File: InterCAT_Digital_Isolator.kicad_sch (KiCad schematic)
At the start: 21 parts

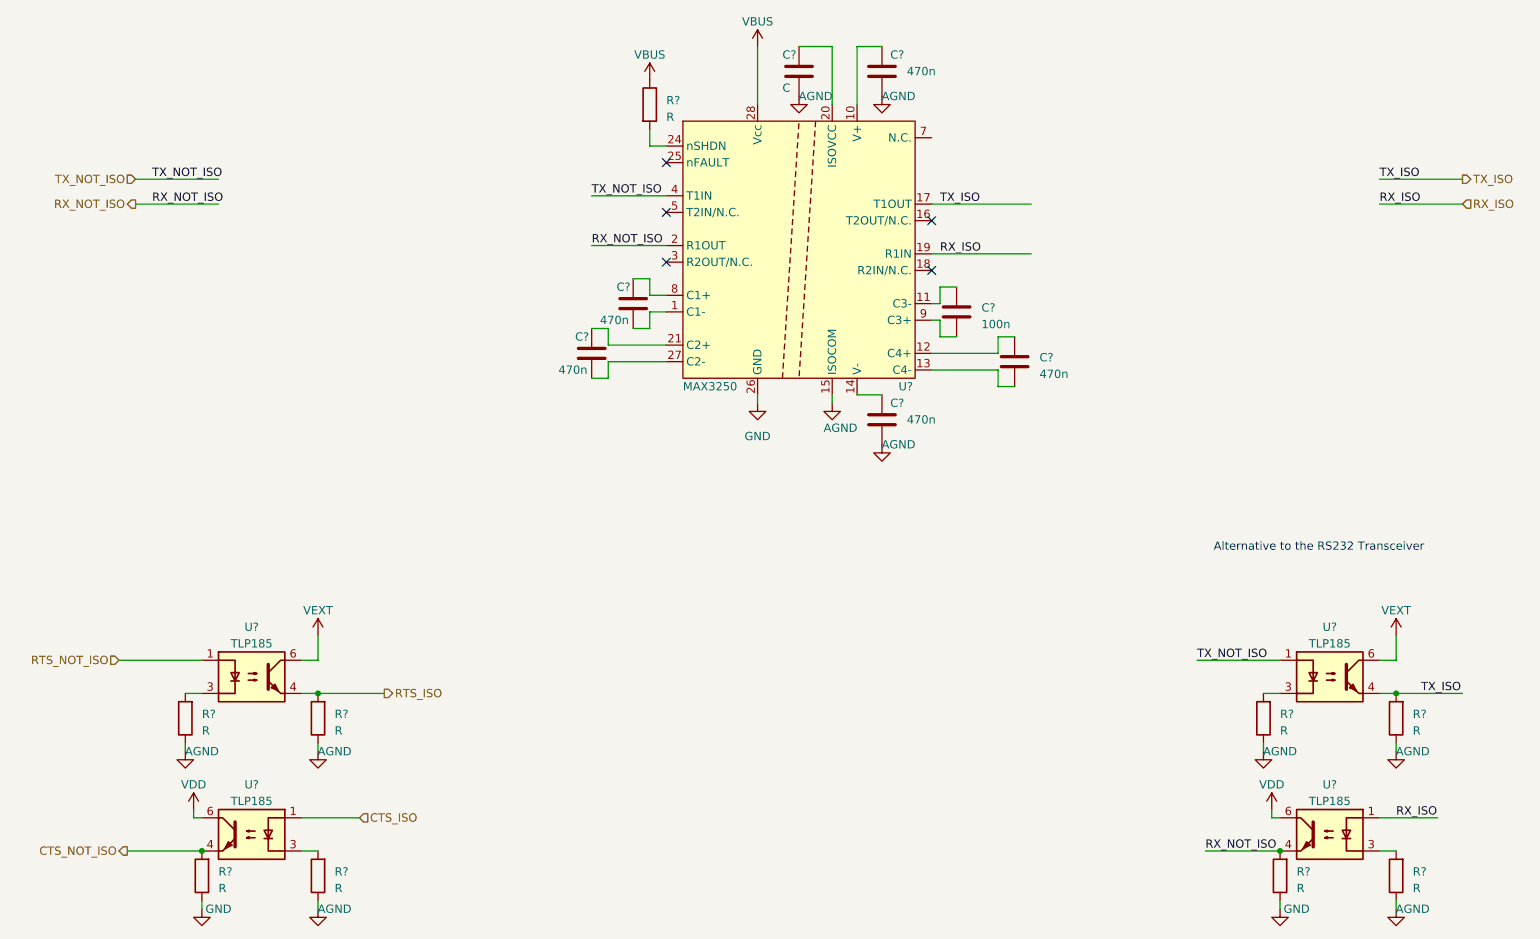
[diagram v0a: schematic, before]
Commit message: Started working on the PCB. alignement in analog channels. changed opamps ot Microchip RRIO basic on LCSC updated footprint on maxim Added LCSC parameter corrected some errors in GND/AGND corrected some errors in VCCA/VCC
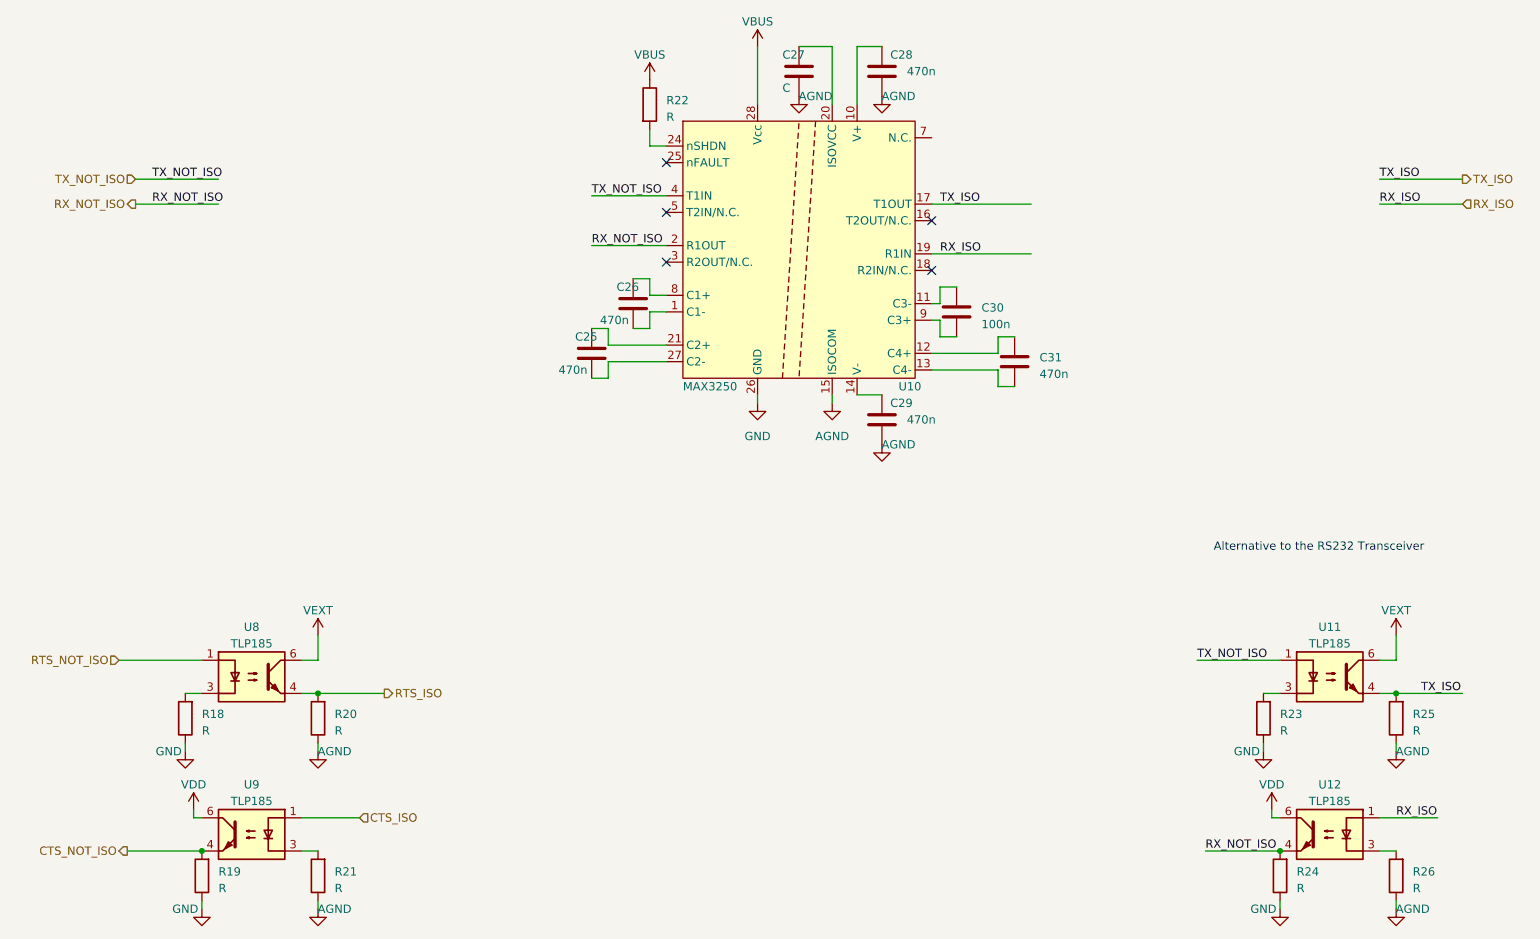
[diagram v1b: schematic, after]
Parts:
- C25, C26, C27, C28, C29, C30, C31: renamed from C?; footprint (none) -> Capacitor_SMD:C_0603_1608Metric
- R18, R19, R20, R21, R22, R23, R24, R25, R26: renamed from R?; footprint (none) -> Resistor_SMD:R_0603_1608Metric
- U10: renamed from U?; footprint Package_SO:SSOP-24_5.3x8.2mm_P0.65mm -> Package_SO:SSOP-28_5.3x10.2mm_P0.65mm
- gave numbers to parts that had none: 4
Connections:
- net GND: now also R18.1, R19.1, R23.1, R24.1; no longer U10.15 (ISOCOM)
- net GNDA: now also U10.15 (ISOCOM); no longer R18.1, R19.1, R23.1, R24.1

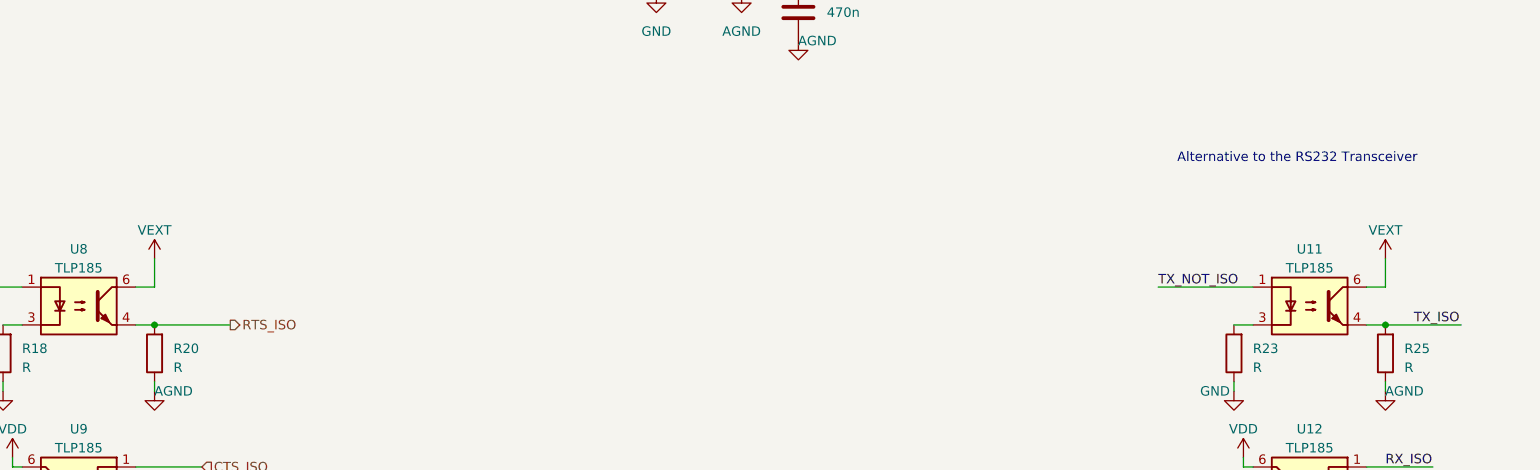
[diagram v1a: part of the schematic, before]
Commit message: Corrected hidden errors in power nets naming
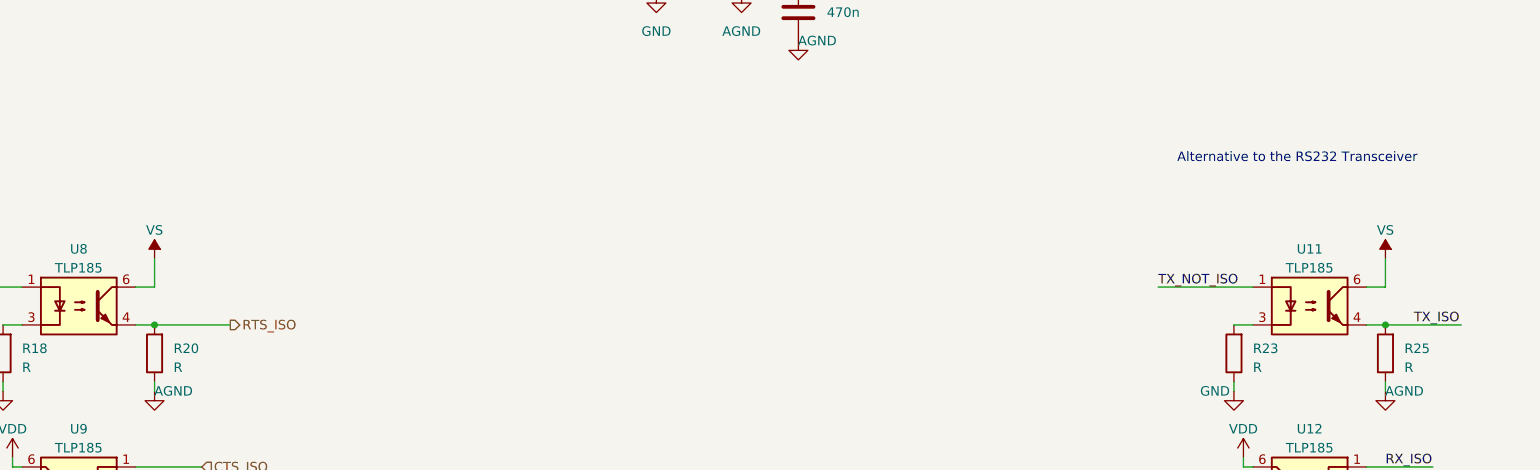
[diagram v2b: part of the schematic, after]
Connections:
- net VBUS: no longer U11.6, U8.6
- new net VS: U11.6, U8.6
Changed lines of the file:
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@@
+    )
+  )
+  (symbol (lib_id "power:VS") (at 243.84 116.84 0) (unit 1)
+    (in_bom yes) (on_board yes) (dnp no) (fields_autoplaced)
+    (property "Reference" "#PWR025" (at 238.76 120.65 0)
+      (effects (font (size 1.27 1.27)) hide)
+    )
+    (property "Value" "VS" (at 243.84 113.03 0)
+      (effects (font (size 1.27 1.27)))
+    )
+    (property "Footprint" "" (at 243.84 116.84 0)
+      (effects (font (size 1.27 1.27)) hide)
+    )
+    (property "Datasheet" "" (at 243.84 116.84 0)
+      (effects (font (size 1.27 1.27)) hide)
+    )
+    (pin "1")
+    (instances
+      (project "Intercat"
+        (path "/03d88a85-11fd-47aa-954c-c318bb15294a"
+          (reference "#PWR025") (unit 1)
+        )
+        (path "/03d88a85-11fd-47aa-954c-c318bb15294a/fcde6974-78be-43f2-8f1f-c3bd2febfa67"
+          (reference "#PWR028") (unit 1)
+        )
+      )
     )
   )
@@
   (symbol (lib_id "power:GND") (at 58.42 134.62 0) (unit 1)
     (in_bom yes) (on_board yes) (dnp no)
-    (property "Reference" "#PWR051" (at 58.42 140.97 0)
+    (property "Reference" "#PWR0133" (at 58.42 140.97 0)
       (effects (font (size 1.27 1.27)) hide)
     )
@@
       (project "Intercat"
         (path "/03d88a85-11fd-47aa-954c-c318bb15294a/fcde6974-78be-43f2-8f1f-c3bd2febfa67"
-          (reference "#PWR051") (unit 1)
+          (reference "#PWR0133") (unit 1)
         )
       )
@@
   (symbol (lib_id "power:GND") (at 226.06 158.75 0) (unit 1)
     (in_bom yes) (on_board yes) (dnp no)
-    (property "Reference" "#PWR066" (at 226.06 165.1 0)
+    (property "Reference" "#PWR0130" (at 226.06 165.1 0)
       (effects (font (size 1.27 1.27)) hide)
     )
@@
       (project "Intercat"
         (path "/03d88a85-11fd-47aa-954c-c318bb15294a/fcde6974-78be-43f2-8f1f-c3bd2febfa67"
-          (reference "#PWR066") (unit 1)
+          (reference "#PWR0130") (unit 1)
         )
       )
@@
   (symbol (lib_id "power:GND") (at 223.52 134.62 0) (unit 1)
     (in_bom yes) (on_board yes) (dnp no)
-    (property "Reference" "#PWR064" (at 223.52 140.97 0)
+    (property "Reference" "#PWR0131" (at 223.52 140.97 0)
       (effects (font (size 1.27 1.27)) hide)
     )
@@
       (project "Intercat"
         (path "/03d88a85-11fd-47aa-954c-c318bb15294a/fcde6974-78be-43f2-8f1f-c3bd2febfa67"
-          (reference "#PWR064") (unit 1)
+          (reference "#PWR0131") (unit 1)
         )
       )
@@
   (symbol (lib_id "power:GND") (at 146.05 81.28 0) (unit 1)
     (in_bom yes) (on_board yes) (dnp no) (fields_autoplaced)
-    (property "Reference" "#PWR059" (at 146.05 87.63 0)
+    (property "Reference" "#PWR0129" (at 146.05 87.63 0)
       (effects (font (size 1.27 1.27)) hide)
     )
@@
       (project "Intercat"
         (path "/03d88a85-11fd-47aa-954c-c318bb15294a/fcde6974-78be-43f2-8f1f-c3bd2febfa67"
-          (reference "#PWR059") (unit 1)
+          (reference "#PWR0129") (unit 1)
         )
       )
@@
     )
   )
-  (symbol (lib_id "power:VBUS") (at 243.84 116.84 0) (unit 1)
-    (in_bom yes) (on_board yes) (dnp no) (fields_autoplaced)
-    (property "Reference" "#PWR067" (at 243.84 120.65 0)
-      (effects (font (size 1.27 1.27)) hide)
-    )
-    (property "Value" "VEXT" (at 243.84 113.03 0)
-      (effects (font (size 1.27 1.27)))
-    )
-    (property "Footprint" "" (at 243.84 116.84 0)
-      (effects (font (size 1.27 1.27)) hide)
-    )
-    (property "Datasheet" "" (at 243.84 116.84 0)
-      (effects (font (size 1.27 1.27)) hide)
-    )
-    (pin "1")
-    (instances
-      (project "Intercat"
-        (path "/03d88a85-11fd-47aa-954c-c318bb15294a/fcde6974-78be-43f2-8f1f-c3bd2febfa67"
-          (reference "#PWR067") (unit 1)
-        )
-      )
-    )
-  )
   (symbol (lib_id "Device:R") (at 243.84 153.67 180) (unit 1)
     (in_bom yes) (on_board yes) (dnp no) (fields_autoplaced)
@@
         (path "/03d88a85-11fd-47aa-954c-c318bb15294a/fcde6974-78be-43f2-8f1f-c3bd2febfa67"
           (reference "C25") (unit 1)
-        )
-      )
-    )
-  )
-  (symbol (lib_id "power:VBUS") (at 78.74 116.84 0) (unit 1)
-    (in_bom yes) (on_board yes) (dnp no) (fields_autoplaced)
-    (property "Reference" "#PWR054" (at 78.74 120.65 0)
-      (effects (font (size 1.27 1.27)) hide)
-    )
-    (property "Value" "VEXT" (at 78.74 113.03 0)
-      (effects (font (size 1.27 1.27)))
-    )
-    (property "Footprint" "" (at 78.74 116.84 0)
-      (effects (font (size 1.27 1.27)) hide)
-    )
-    (property "Datasheet" "" (at 78.74 116.84 0)
-      (effects (font (size 1.27 1.27)) hide)
-    )
-    (pin "1")
-    (instances
-      (project "Intercat"
-        (path "/03d88a85-11fd-47aa-954c-c318bb15294a/fcde6974-78be-43f2-8f1f-c3bd2febfa67"
-          (reference "#PWR054") (unit 1)
         )
       )
@@
   (symbol (lib_id "power:GND") (at 60.96 158.75 0) (unit 1)
     (in_bom yes) (on_board yes) (dnp no)
-    (property "Reference" "#PWR053" (at 60.96 165.1 0)
+    (property "Reference" "#PWR0132" (at 60.96 165.1 0)
       (effects (font (size 1.27 1.27)) hide)
     )
@@
       (project "Intercat"
         (path "/03d88a85-11fd-47aa-954c-c318bb15294a/fcde6974-78be-43f2-8f1f-c3bd2febfa67"
-          (reference "#PWR053") (unit 1)
+          (reference "#PWR0132") (unit 1)
         )
       )
@@
         )
       )
+    )
+  )
+  (symbol (lib_id "power:VS") (at 78.74 116.84 0) (unit 1)
+    (in_bom yes) (on_board yes) (dnp no) (fields_autoplaced)
+    (property "Reference" "#PWR025" (at 73.66 120.65 0)
+      (effects (font (size 1.27 1.27)) hide)
+    )
+    (property "Value" "VS" (at 78.74 113.03 0)
+      (effects (font (size 1.27 1.27)))
+    )
+    (property "Footprint" "" (at 78.74 116.84 0)
+      (effects (font (size 1.27 1.27)) hide)
+    )
+    (property "Datasheet" "" (at 78.74 116.84 0)
+      (effects (font (size 1.27 1.27)) hide)
+    )
+    (pin "1")
+    (instances
+      (project "Intercat"
+        (path "/03d88a85-11fd-47aa-954c-c318bb15294a"
+          (reference "#PWR025") (unit 1)
+        )
+        (path "/03d88a85-11fd-47aa-954c-c318bb15294a/fcde6974-78be-43f2-8f1f-c3bd2febfa67"
+          (reference "#PWR054") (unit 1)
+        )
+      )

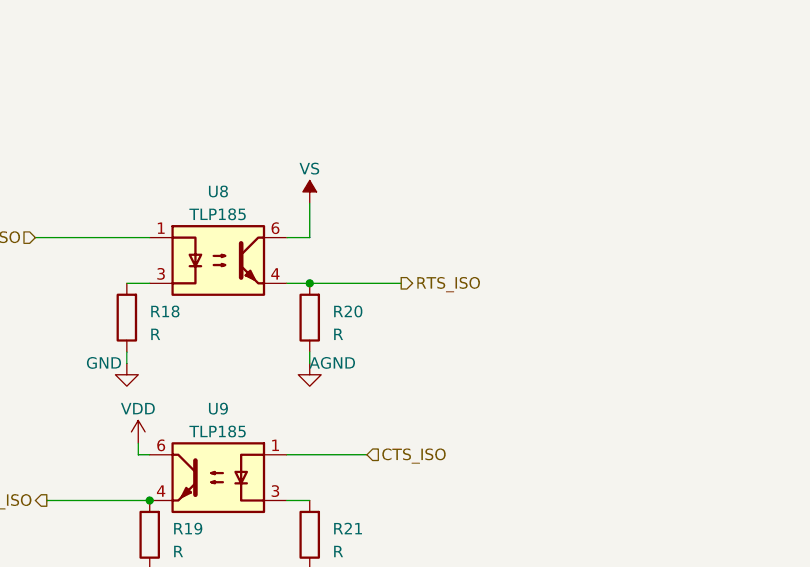
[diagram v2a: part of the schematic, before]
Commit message: removed jack connectors, added testpoints on DAC
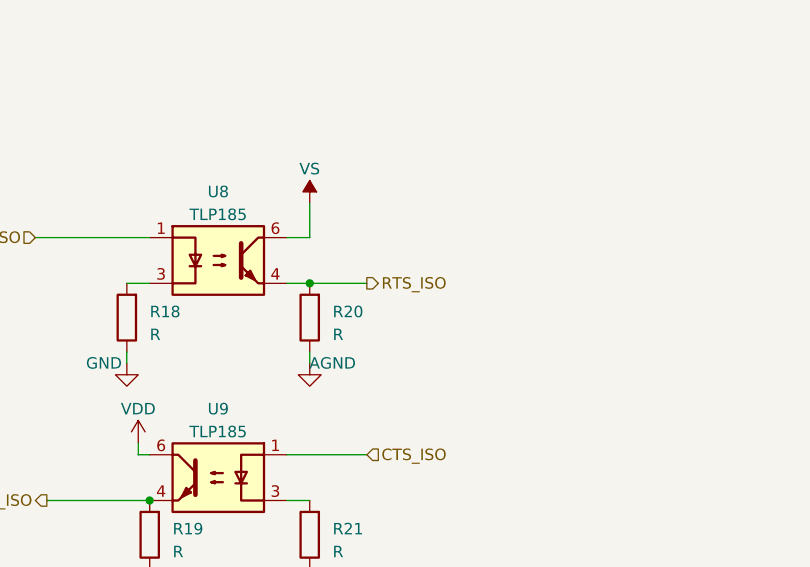
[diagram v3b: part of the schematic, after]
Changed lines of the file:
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@@
     (stroke (width 0) (type default))
   )
-  (wire (pts (xy 78.74 125.73) (xy 88.9 125.73))
+  (wire (pts (xy 78.74 125.73) (xy 85.09 125.73))
     (stroke (width 0) (type default))
   )
@@
     (effects (font (size 1.27 1.27)) (justify right))
   )
-  (hierarchical_label "RTS_ISO" (shape output) (at 88.9 125.73 0) (fields_autoplaced)
+  (hierarchical_label "RTS_ISO" (shape output) (at 85.09 125.73 0) (fields_autoplaced)
     (effects (font (size 1.27 1.27)) (justify left))
   )
